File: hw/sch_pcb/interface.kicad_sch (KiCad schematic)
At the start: 24 parts, among them J6 HEADER_2x15, U12 MIC5504-3.3YM5-TR, U12 SN74LVC2T45DCU, U13 SN74LVC2T45DCU, U14 SN74LVC2T45DCU, U6 AT24CS64-SSHM

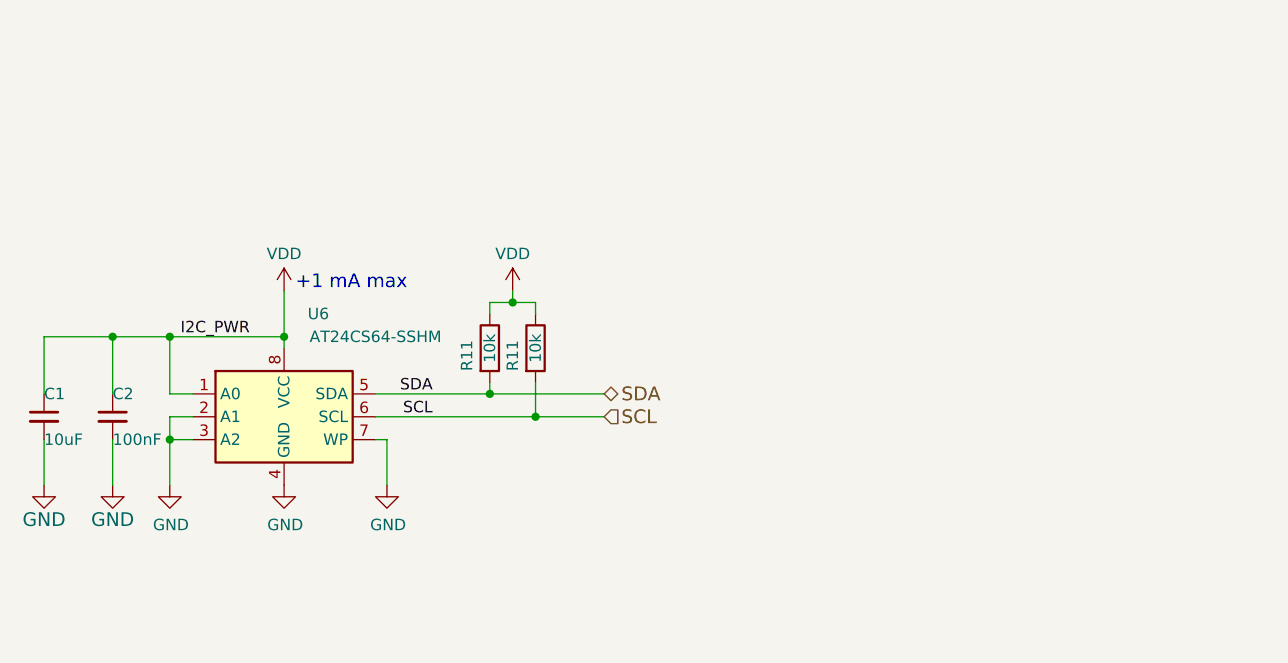
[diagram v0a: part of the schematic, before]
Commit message: Fix #8 Adding solder jumpers.
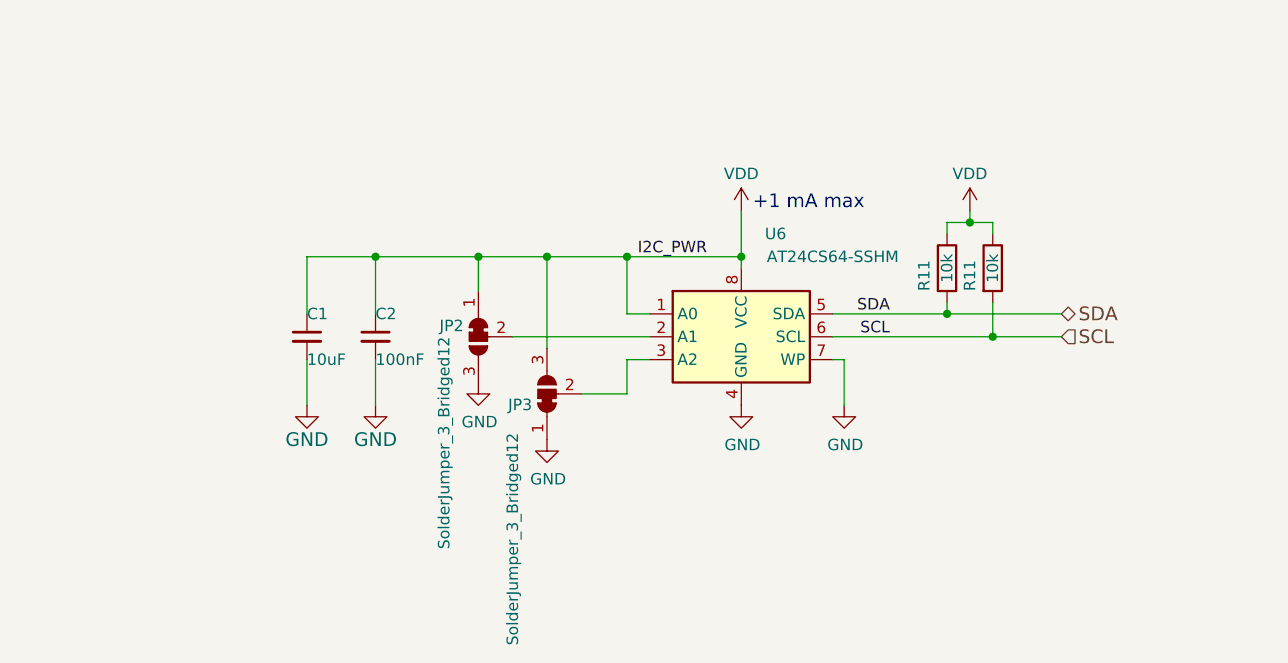
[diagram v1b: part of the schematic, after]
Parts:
- added JP2, JP3: SolderJumper_3_Bridged12, Jumper:SolderJumper-3_P1.3mm_Bridged12_RoundedPad1.0x1.5mm, symbol Jumper:SolderJumper_3_Bridged12
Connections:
- net GND: now also JP2.3 (B), JP3.1 (A); no longer U6.2 (A1), U6.3 (A2)
- net VDD: now also JP2.1 (A), JP3.3 (B)
- new net: JP2.2 (C), U6.2 (A1)
- new net: JP3.2 (C), U6.3 (A2)
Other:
- moved on the sheet: C1, C2, R11, U6

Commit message: Resolve #10
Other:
- title: USTSIPIN03B -> USTSIPIN03C
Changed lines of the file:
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@@
 	(paper "A4")
 	(title_block
-		(title "USTSIPIN03B")
+		(title "USTSIPIN03C")
 		(date "2023-10-23")
 		(company "kaklik <info@ust.cz>")

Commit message: Update KiCAD project.
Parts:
- renumbered C2 to C38, C1 to C40, C2 to C41, C2 to C42, C2 to C43, C2 to C44, C2 to C45, C2 to C46, C2 to C47, C41 to C49, C46 to C50, C49 to C51, C51 to C52, J6 to J1, L4 to L1, R11 to R29, R11 to R30, U6 to U11, U12 to U15
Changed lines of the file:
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@@
 (kicad_sch
-	(version 20231120)
+	(version 20250114)
 	(generator "eeschema")
-	(generator_version "8.0")
+	(generator_version "9.0")
 	(paper "A4")
 	(title_block
@@
 		(comment 2 "Semiconductor\\nionizing radiation detector")
 	)
+	(text "+1 mA max"
+		(exclude_from_sim no)
+		(at 101.6 142.24 0)
+		(effects
+			(font
+				(size 1.524 1.524)
+			)
+			(justify left bottom)
+		)
+	)
+	(text "16 μA"
+		(exclude_from_sim no)
+		(at 154.94 72.39 0)
+		(effects
+			(font
+				(size 1.27 1.27)
+			)
+			(justify left bottom)
+		)
+	)
+	(text "16 μA"
+		(exclude_from_sim no)
+		(at 62.23 72.39 0)
+		(effects
+			(font
+				(size 1.524 1.524)
+			)
+			(justify left bottom)
+		)
+	)
+	(text "POWER INPUT 5.5 mA "
+		(exclude_from_sim no)
+		(at 207.01 34.29 0)
+		(effects
+			(font
+				(size 1.524 1.524)
+			)
+			(justify left bottom)
+		)
+	)
+	(text "16 μA"
+		(exclude_from_sim no)
+		(at 106.68 72.39 0)
+		(effects
+			(font
+				(size 1.27 1.27)
+			)
+			(justify left bottom)
+		)
+	)
 	(junction
 		(at 100.33 147.32)
@@
 		)
 	)
-	(text "+1 mA max"
-		(exclude_from_sim no)
-		(at 101.6 142.24 0)
-		(effects
-			(font
-				(size 1.524 1.524)
-			)
-			(justify left bottom)
-		)
-	)
-	(text "16 μA"
-		(exclude_from_sim no)
-		(at 154.94 72.39 0)
-		(effects
-			(font
-				(size 1.27 1.27)
-			)
-			(justify left bottom)
-		)
-	)
-	(text "16 μA"
-		(exclude_from_sim no)
-		(at 62.23 72.39 0)
-		(effects
-			(font
-				(size 1.524 1.524)
-			)
-			(justify left bottom)
-		)
-	)
-	(text "POWER INPUT 5.5 mA "
-		(exclude_from_sim no)
-		(at 207.01 34.29 0)
-		(effects
-			(font
-				(size 1.524 1.524)
-			)
-			(justify left bottom)
-		)
-	)
-	(text "16 μA"
-		(exclude_from_sim no)
-		(at 106.68 72.39 0)
-		(effects
-			(font
-				(size 1.27 1.27)
-			)
-			(justify left bottom)
-		)
-	)
 	(label "RX"
 		(at 241.3 74.93 270)
@@
 		(on_board yes)
 		(dnp no)
-		(property "Reference" "#PWR0106"
+		(property "Reference" "#PWR096"
 			(at 55.88 76.2 0)
 			(effects
@@
 		(on_board yes)
 		(dnp no)
-		(property "Reference" "#PWR0106"
+		(property "Reference" "#PWR092"
 			(at 147.32 76.2 0)
 			(effects
@@
 		(dnp no)
 		(fields_autoplaced yes)
-		(property "Reference" "L4"
+		(property "Reference" "L1"
 			(at 181.61 31.7967 90)
 			(effects
@@
 		(dnp no)
 		(fields_autoplaced yes)
-		(property "Reference" "#PWR0162"
+		(property "Reference" "#PWR062"
 			(at 228.6 52.07 0)
 			(effects
@@
 		(on_board yes)
 		(dnp no)
-		(property "Reference" "#PWR039"
+		(property "Reference" "#PWR089"
 			(at 41.91 52.07 0)
 			(effects
@@
 		(on_board yes)
 		(dnp no)
-		(property "Reference" "#PWR0169"
+		(property "Reference" "#PWR066"
 			(at 254 93.98 0)
 			(effects
@@
 		(on_board yes)
 		(dnp no)
-		(property "Reference" "#PWR028"
+		(property "Reference" "#PWR070"
 			(at 78.74 173.99 0)
 			(effects
@@
 		(on_board yes)
 		(dnp no)
-		(property "Reference" "C2"
+		(property "Reference" "C45"
 			(at 118.11 76.2 0)
 			(effects
@@
 		(on_board yes)
 		(dnp no)
-		(property "Reference" "#PWR0168"
+		(property "Reference" "#PWR061"
 			(at 254 44.45 0)
 			(effects
@@
 		(dnp no)
 		(fields_autoplaced yes)
-		(property "Reference" "#PWR018"
+		(property "Reference" "#PWR067"
 			(at 100.33 146.05 0)
 			(effects
@@
 		(dnp no)
 		(fields_autoplaced yes)
-		(property "Reference" "#PWR0164"
+		(property "Reference" "#PWR065"
 			(at 228.6 86.36 0)
 			(effects
@@
 		(on_board yes)
 		(dnp no)
-		(property "Reference" "#PWR030"
+		(property "Reference" "#PWR071"
 			(at 100.33 170.18 0)
 			(effects
@@
 		(on_board yes)
 		(dnp no)
-		(property "Reference" "#PWR015"
+		(property "Reference" "#PWR075"
 			(at 55.88 88.9 0)
 			(effects
@@
 		(dnp no)
 		(fields_autoplaced yes)
-		(property "Reference" "#PWR0164"
+		(property "Reference" "#PWR074"
 			(at 66.04 119.38 0)
 			(effects
@@
 		(on_board yes)
 		(dnp no)
-		(property "Reference" "C2"
+		(property "Reference" "C38"
 			(at 204.47 40.64 0)
 			(effects
@@
 		(on_board yes)
 		(dnp no)
-		(property "Reference" "C2"
+		(property "Reference" "C43"
 			(at 74.93 76.2 0)
 			(effects
@@
 		(on_board yes)
 		(dnp no)
-		(property "Reference" "#PWR0152"
+		(property "Reference" "#PWR057"
 			(at 172.72 31.75 0)
 			(effects
@@
 		(on_board yes)
 		(dnp no)
-		(property "Reference" "#PWR0106"
+		(property "Reference" "#PWR085"
 			(at 100.33 33.02 0)
 			(effects
@@
 		(dnp no)
 		(fields_autoplaced yes)
-		(property "Reference" "#PWR0164"
+		(property "Reference" "#PWR079"
 			(at 109.22 119.38 0)
 			(effects
@@
 		(on_board yes)
 		(dnp no)
-		(property "Reference" "#PWR015"
+		(property "Reference" "#PWR077"
 			(at 99.06 88.9 0)
 			(effects
@@
 		(dnp no)
 		(fields_autoplaced yes)
-		(property "Reference" "#PWR018"
+		(property "Reference" "#PWR073"
 			(at 125.73 146.05 0)
 			(effects
@@
 		(on_board yes)
 		(dnp no)
-		(property "Reference" "C49"
+		(property "Reference" "C51"
 			(at 93.091 38.2016 0)
 			(effects
@@
 		(on_board yes)
 		(dnp no)
-		(property "Reference" "C1"
+		(property "Reference" "C40"
 			(at 52.07 153.67 0)
 			(effects
@@
 		(on_board yes)
 		(dnp no)
-		(property "Reference" "#PWR0163"
+		(property "Reference" "#PWR064"
 			(at 264.16 83.82 0)
 			(effects
@@
 		(on_board yes)
 		(dnp no)
-		(property "Reference" "C46"
+		(property "Reference" "C50"
 			(at 56.2611 36.9506 0)
 			(effects
@@
 		(on_board yes)
 		(dnp no)
-		(property "Reference" "R11"
+		(property "Reference" "R29"
 			(at 120.65 151.13 90)
 			(effects
@@
 		(on_board yes)
 		(dnp no)
-		(property "Reference" "C51"
+		(property "Reference" "C52"
 			(at 103.251 38.2016 0)
 			(effects
@@
 		(on_board yes)
 		(dnp no)
-		(property "Reference" "C2"
+		(property "Reference" "C46"
 			(at 144.78 77.47 0)
 			(effects
@@
 		(on_board yes)
 		(dnp no)
-		(property "Reference" "#PWR0111"
+		(property "Reference" "#PWR088"
 			(at 100.33 50.8 0)
 			(effects
@@
 		(on_board yes)
 		(dnp no)
-		(property "Reference" "C2"
+		(property "Reference" "C42"
 			(at 55.88 76.2 0)
 			(effects
@@
 		(dnp no)
 		(fields_autoplaced yes)
-		(property "Reference" "#PWR0164"
+		(property "Reference" "#PWR082"
 			(at 157.48 119.38 0)
 			(effects
@@
 		(on_board yes)
 		(dnp no)
-		(property "Reference" "R11"
+		(property "Reference" "R30"
 			(at 125.73 151.13 90)
 			(effects
@@
 		(on_board yes)
 		(dnp no)
-		(property "Reference" "#PWR015"
+		(property "Reference" "#PWR080"
 			(at 147.32 88.9 0)
 			(effects
@@
 		(on_board yes)
 		(dnp no)
-		(property "Reference" "#PWR0110"
+		(property "Reference" "#PWR087"
 			(at 90.17 50.8 0)
 			(effects
@@
 		(on_board yes)
 		(dnp no)
-		(property "Reference" "#PWR015"
+		(property "Reference" "#PWR081"
 			(at 166.37 88.9 0)
 			(effects
@@
 		(on_board yes)
 		(dnp no)
-		(property "Reference" "#PWR015"
+		(property "Reference" "#PWR078"
 			(at 118.11 88.9 0)
 			(effects
@@
 		(on_board yes)
 		(dnp no)
-		(property "Reference" "#PWR031"
+		(property "Reference" "#PWR072"
 			(at 111.76 170.18 0)
 			(effects
@@
 		(on_board yes)
 		(dnp no)
-		(property "Reference" "C41"
+		(property "Reference" "C49"
 			(at 44.8311 36.9506 0)
 			(effects
@@
 		(on_board yes)
 		(dnp no)
-		(property "Reference" "#PWR015"
+		(property "Reference" "#PWR069"
 			(at 59.69 170.18 0)
 			(effects
@@
 		(on_board yes)
 		(dnp no)
-		(property "Reference" "C2"
+		(property "Reference" "C47"
 			(at 168.91 77.47 0)
 			(effects
@@
 		(on_board yes)
 		(dnp no)
-		(property "Reference" "#PWR0107"
+		(property "Reference" "#PWR086"
 			(at 76.2 50.8 0)
 			(effects
@@
 		(on_board yes)
 		(dnp no)
-		(property "Reference" "C2"
+		(property "Reference" "C41"
 			(at 59.69 153.67 0)
 			(effects
@@
 		(on_board yes)
 		(dnp no)
-		(property "Reference" "#PWR015"
+		(property "Reference" "#PWR076"
 			(at 74.93 88.9 0)
 			(effects
@@
 		(on_board yes)
 		(dnp no)
-		(property "Reference" "#PWR015"
+		(property "Reference" "#PWR068"
 			(at 52.07 170.18 0)
 			(effects
@@
 		(on_board yes)
 		(dnp no)
-		(property "Reference" "#PWR041"
+		(property "Reference" "#PWR090"
 			(at 53.34 52.07 0)
 			(effects
@@
 		(on_board yes)
 		(dnp no)
-		(property "Reference" "#PWR0106"
+		(property "Reference" "#PWR095"
 			(at 99.06 76.2 0)
 			(effects
@@
 		(on_board yes)
 		(dnp no)
-		(property "Reference" "J6"
+		(property "Reference" "J1"
 			(at 226.06 69.85 90)
 			(effects
@@
 		(on_board yes)
 		(dnp no)
-		(property "Reference" "U12"
+		(property "Reference" "U15"
 			(at 76.2 26.2382 0)
 			(effects
@@
 		(on_board yes)
 		(dnp no)
-		(property "Reference" "#PWR0161"
+		(property "Reference" "#PWR063"
 			(at 264.16 53.34 0)
 			(effects
@@
 		(on_board yes)
 		(dnp no)
-		(property "Reference" "C2"
+		(property "Reference" "C44"
 			(at 99.06 76.2 0)
 			(effects
@@
 		(on_board yes)
 		(dnp no)
-		(property "Reference" "U6"
+		(property "Reference" "U11"
 			(at 104.14 144.78 0)
 			(effects
